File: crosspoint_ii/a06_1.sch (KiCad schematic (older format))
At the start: 38 parts, among them U6001 74HC27, U6002 74HC02, U6003 74HC27, U6004 74LVC07, U6005 74HC02, U6006 74HC04, U6007 74HC27, U6008 74HC27, U6009 74HC02, U6010 74HC04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

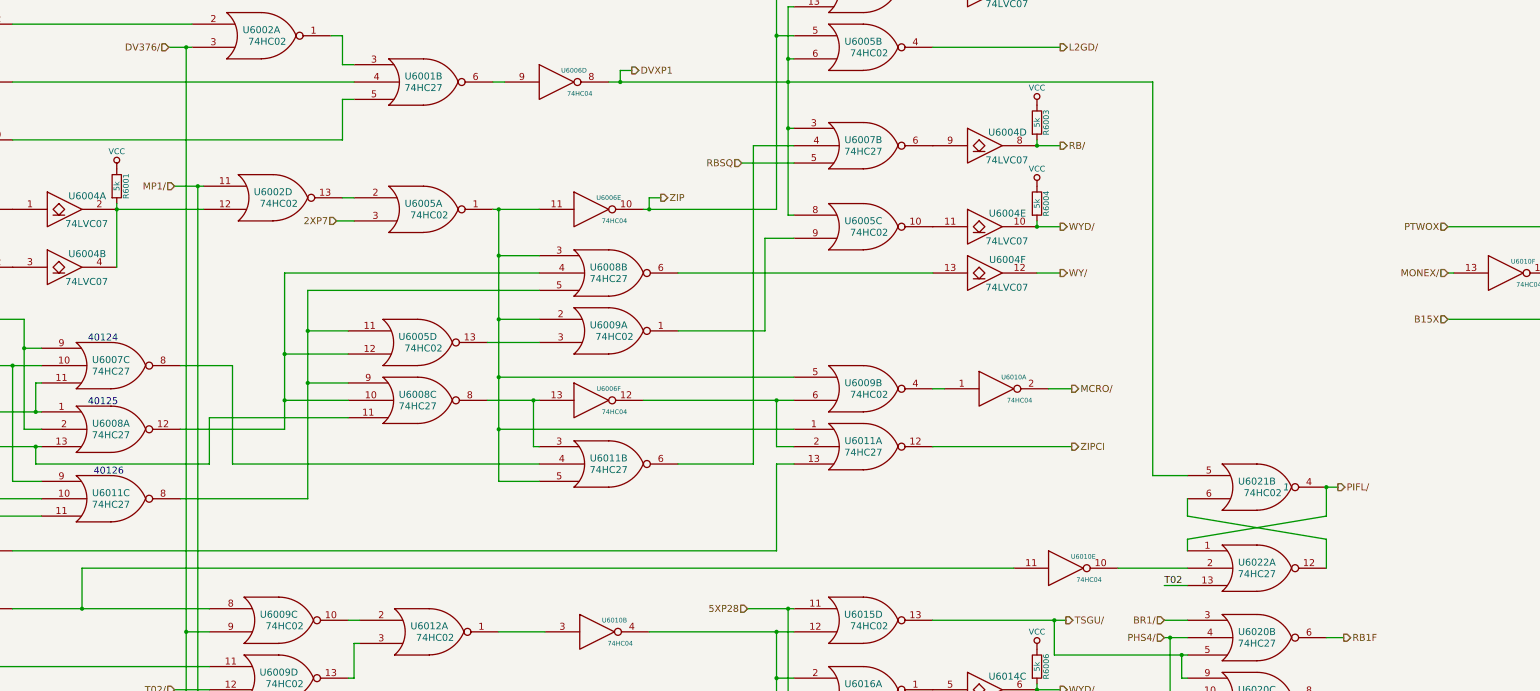
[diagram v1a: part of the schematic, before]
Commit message: Tied in module 6 and corrected a handful of naming/routing errors... most notably some missing gates from A06-1
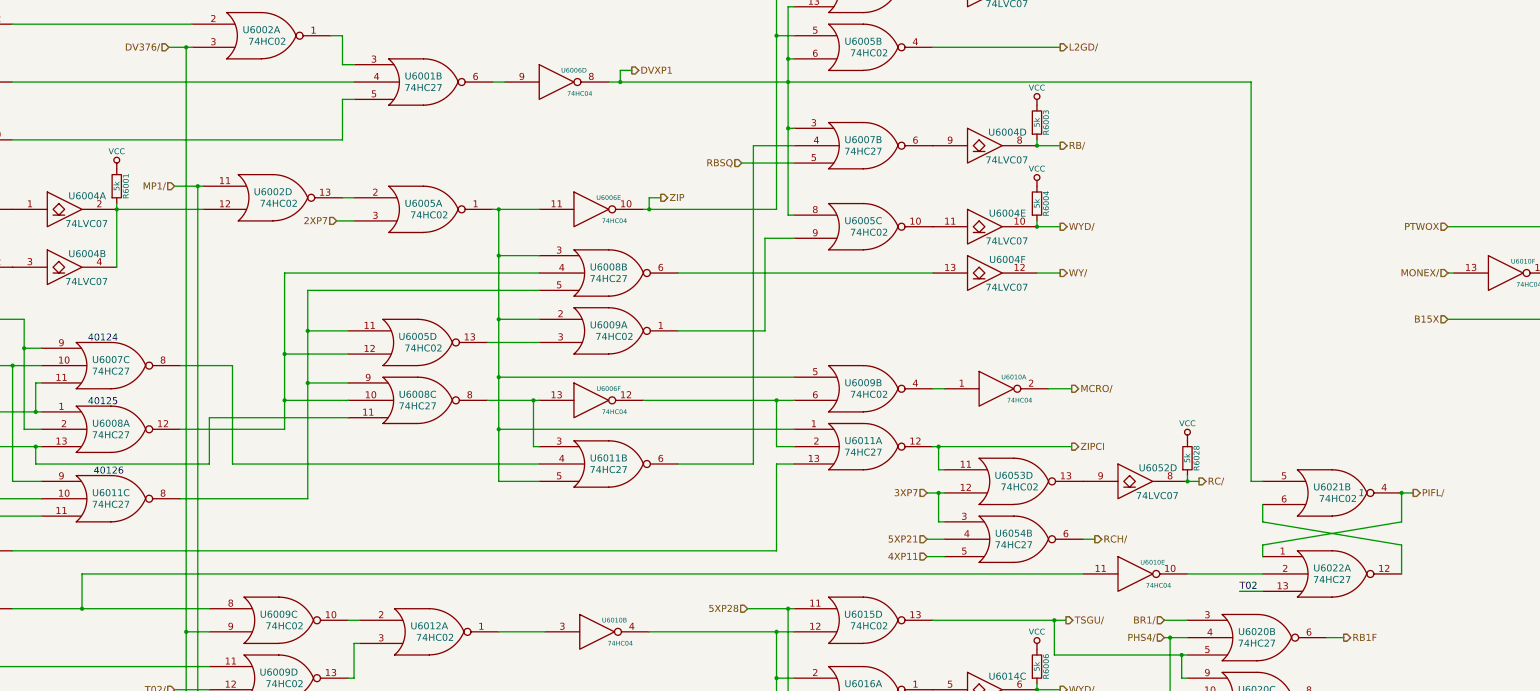
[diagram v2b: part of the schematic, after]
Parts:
- added R6028: 5k, symbol R
- added U6052: 74LVC07, symbol 74LVC07
- added U6053: 74HC02, symbol 74HC02
- added U6054: 74HC27, symbol 74HC27
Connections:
- net GND: now also U6052.7 (GND), U6053.7 (GND), U6054.7 (GND)
- net VCC: now also R6028.1, U6052.14 (VCC), U6053.14 (VCC), U6054.14 (VCC)
- net ZIPCI: now also U6053.11
- new net: U6052.9, U6053.13
- new net 3XP7: U6053.12, U6054.3
- new net 4XP11: U6054.5
- new net 5XP21: U6054.4
- new net RC/: R6028.2, U6052.8
- new net RCH/: U6054.6
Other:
- moved on the sheet: U6010E, U6021B, U6022A
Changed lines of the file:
@@
 $EndComp
 $Comp
-L VCC #PWR07
+L VCC #PWR03
 U 1 1 5687E325
 P 4400 2600
-F 0 "#PWR07" H 4400 2450 50  0001 C CNN
+F 0 "#PWR03" H 4400 2450 50  0001 C CNN
 F 1 "VCC" H 4400 2750 50  0000 C CNN
 F 2 "" H 4400 2600 60  0000 C CNN
@@
 $EndComp
 $Comp
-L VCC #PWR08
+L VCC #PWR04
 U 1 1 56881A2B
 P 12350 700
-F 0 "#PWR08" H 12350 550 50  0001 C CNN
+F 0 "#PWR04" H 12350 550 50  0001 C CNN
 F 1 "VCC" H 12350 850 50  0000 C CNN
 F 2 "" H 12350 700 60  0000 C CNN
@@
 $EndComp
 $Comp
-L VCC #PWR09
+L VCC #PWR05
 U 1 1 56883547
 P 12350 2050
-F 0 "#PWR09" H 12350 1900 50  0001 C CNN
+F 0 "#PWR05" H 12350 1900 50  0001 C CNN
 F 1 "VCC" H 12350 2200 50  0000 C CNN
 F 2 "" H 12350 2050 60  0000 C CNN
@@
 $EndComp
 $Comp
-L VCC #PWR010
+L VCC #PWR06
 U 1 1 56884333
 P 12350 2750
-F 0 "#PWR010" H 12350 2600 50  0001 C CNN
+F 0 "#PWR06" H 12350 2600 50  0001 C CNN
 F 1 "VCC" H 12350 2900 50  0000 C CNN
 F 2 "" H 12350 2750 60  0000 C CNN
@@
 $EndComp
 $Comp
-L VCC #PWR011
+L VCC #PWR07
 U 1 1 568AA059
 P 4400 7950
-F 0 "#PWR011" H 4400 7800 50  0001 C CNN
+F 0 "#PWR07" H 4400 7800 50  0001 C CNN
 F 1 "VCC" H 4400 8100 50  0000 C CNN
 F 2 "" H 4400 7950 60  0000 C CNN
@@
 $EndComp
 $Comp
-L VCC #PWR012
+L VCC #PWR08
 U 1 1 568B96C1
 P 12350 6750
-F 0 "#PWR012" H 12350 6600 50  0001 C CNN
+F 0 "#PWR08" H 12350 6600 50  0001 C CNN
 F 1 "VCC" H 12350 6900 50  0000 C CNN
 F 2 "" H 12350 6750 60  0000 C CNN
@@
 $EndComp
 $Comp
-L VCC #PWR013
+L VCC #PWR09
 U 1 1 568BD3AF
 P 12350 7500
-F 0 "#PWR013" H 12350 7350 50  0001 C CNN
+F 0 "#PWR09" H 12350 7350 50  0001 C CNN
 F 1 "VCC" H 12350 7650 50  0000 C CNN
 F 2 "" H 12350 7500 60  0000 C CNN
@@
 $EndComp
 $Comp
-L VCC #PWR014
+L VCC #PWR010
 U 1 1 568BF167
 P 12350 8200
-F 0 "#PWR014" H 12350 8050 50  0001 C CNN
+F 0 "#PWR010" H 12350 8050 50  0001 C CNN
 F 1 "VCC" H 12350 8350 50  0000 C CNN
 F 2 "" H 12350 8200 60  0000 C CNN
@@
 $EndComp
 $Comp
-L VCC #PWR015
+L VCC #PWR011
 U 1 1 568BFF2A
 P 12350 8900
-F 0 "#PWR015" H 12350 8750 50  0001 C CNN
+F 0 "#PWR011" H 12350 8750 50  0001 C CNN
 F 1 "VCC" H 12350 9050 50  0000 C CNN
 F 2 "" H 12350 8900 60  0000 C CNN
@@
 $EndComp
 $Comp
-L VCC #PWR016
+L VCC #PWR012
 U 1 1 568D20A8
 P 12350 9600
-F 0 "#PWR016" H 12350 9450 50  0001 C CNN
+F 0 "#PWR012" H 12350 9450 50  0001 C CNN
 F 1 "VCC" H 12350 9750 50  0000 C CNN
 F 2 "" H 12350 9600 60  0000 C CNN
@@
 	10200 1200 10200 3000
 Wire Wire Line
-	8650 1850 13350 1850
+	8650 1850 14200 1850
 Wire Wire Line
 	10200 1650 10250 1650
@@
 $EndComp
 $Comp
-L VCC #PWR017
+L VCC #PWR013
 U 1 1 568E688E
 P 12350 10700
-F 0 "#PWR017" H 12350 10550 50  0001 C CNN
+F 0 "#PWR013" H 12350 10550 50  0001 C CNN
 F 1 "VCC" H 12350 10850 50  0000 C CNN
 F 2 "" H 12350 10700 60  0000 C CNN
@@
 $EndComp
 $Comp
-L VCC #PWR018
+L VCC #PWR014
 U 1 1 568E71E1
 P 12350 11400
-F 0 "#PWR018" H 12350 11250 50  0001 C CNN
+F 0 "#PWR014" H 12350 11250 50  0001 C CNN
 F 1 "VCC" H 12350 11550 50  0000 C CNN
 F 2 "" H 12350 11400 60  0000 C CNN
@@
 $EndComp
 $Comp
-L VCC #PWR019
+L VCC #PWR015
 U 1 1 568E86FE
 P 12350 12100
-F 0 "#PWR019" H 12350 11950 50  0001 C CNN
+F 0 "#PWR015" H 12350 11950 50  0001 C CNN
 F 1 "VCC" H 12350 12250 50  0000 C CNN
 F 2 "" H 12350 12100 60  0000 C CNN
@@
 DVXP1
 Wire Wire Line
-	4100 6400 4100 6050
-Wire Wire Line
-	4100 6050 12150 6050
+	4100 6400 4100 6100
+Wire Wire Line
+	4100 6100 12750 6100
 Connection ~ 4100 6400
 Wire Wire Line
@@
 L 74HC04 U6010
 U 5 1 568FA6F1
-P 12600 6050
-F 0 "U6010" H 12750 6150 40  0000 C CNN
-F 1 "74HC04" H 12800 5950 40  0000 C CNN
-F 2 "" H 12600 6050 60  0000 C CNN
-F 3 "" H 12600 6050 60  0000 C CNN
-	5    12600 6050
+P 13200 6100
+F 0 "U6010" H 13350 6200 40  0000 C CNN
+F 1 "74HC04" H 13400 6000 40  0000 C CNN
+F 2 "" H 13200 6100 60  0000 C CNN
+F 3 "" H 13200 6100 60  0000 C CNN
+	5    13200 6100
 	1    0    0    -1
 $EndComp
@@
 L 74HC27 U6022
 U 1 1 568FE0E3
-P 14250 6050
-F 0 "U6022" H 14250 6100 60  0000 C CNN
-F 1 "74HC27" H 14250 6000 60  0000 C CNN
-F 2 "" H 14250 6050 60  0000 C CNN
-F 3 "" H 14250 6050 60  0000 C CNN
-	1    14250 6050
-	1    0    0    -1
-$EndComp
-Wire Wire Line
-	13050 6050 13650 6050
-Wire Wire Line
-	13650 6200 13450 6200
-Text Label 13450 6200 0    60   ~ 0
+P 14900 6100
+F 0 "U6022" H 14900 6150 60  0000 C CNN
+F 1 "74HC27" H 14900 6050 60  0000 C CNN
+F 2 "" H 14900 6100 60  0000 C CNN
+F 3 "" H 14900 6100 60  0000 C CNN
+	1    14900 6100
+	1    0    0    -1
+$EndComp
+Wire Wire Line
+	13650 6100 14300 6100
+Wire Wire Line
+	14300 6250 14100 6250
+Text Label 14100 6250 0    60   ~ 0
 T02
 $Comp
 L 74HC02 U6021
 U 2 1 569094BF
-P 14250 5350
-F 0 "U6021" H 14250 5400 60  0000 C CNN
-F 1 "74HC02" H 14300 5300 60  0000 C CNN
-F 2 "" H 14250 5350 60  0000 C CNN
-F 3 "" H 14250 5350 60  0000 C CNN
-F 4 "1" H 14500 5350 60  0000 C CIN "Initial"
-	2    14250 5350
-	1    0    0    -1
-$EndComp
-Wire Wire Line
-	14850 6050 14850 5800
-Wire Wire Line
-	14850 5800 13650 5600
-Wire Wire Line
-	13650 5600 13650 5450
-Wire Wire Line
-	14850 5350 14850 5600
-Wire Wire Line
-	14850 5600 13650 5800
-Wire Wire Line
-	13650 5800 13650 5900
+P 14900 5400
+F 0 "U6021" H 14900 5450 60  0000 C CNN
+F 1 "74HC02" H 14950 5350 60  0000 C CNN
+F 2 "" H 14900 5400 60  0000 C CNN
+F 3 "" H 14900 5400 60  0000 C CNN
+F 4 "1" H 15150 5400 60  0000 C CIN "Initial"
+	2    14900 5400
+	1    0    0    -1
+$EndComp
+Wire Wire Line
+	15500 6100 15500 5850
+Wire Wire Line
+	15500 5850 14300 5650
+Wire Wire Line
+	14300 5650 14300 5500
+Wire Wire Line
+	15500 5400 15500 5650
+Wire Wire Line
+	15500 5650 14300 5850
+Wire Wire Line
+	14300 5850 14300 5950
 Connection ~ 8750 1850
 Connection ~ 10200 1850
 Wire Wire Line
-	13350 1850 13350 5250
-Wire Wire Line
-	13350 5250 13650 5250
-Wire Wire Line
-	14850 5350 14950 5350
-Connection ~ 14850 5350
-Text HLabel 14950 5350 2    60   Output ~ 0
+	14200 1850 14200 5300
+Wire Wire Line
+	14200 5300 14300 5300
+Wire Wire Line
+	15500 5400 15600 5400
+Connection ~ 15500 5400
+Text HLabel 15600 5400 2    60   Output ~ 0
 PIFL/
 $Comp
@@
 Text HLabel 16350 7850 2    60   Output ~ 0
 CGMC
+$Comp
+L 74HC02 U6053
+U 4 1 56A22E56
+P 12150 5300
+F 0 "U6053" H 12150 5350 60  0000 C CNN
+F 1 "74HC02" H 12200 5250 60  0000 C CNN
+F 2 "" H 12150 5300 60  0000 C CNN
+F 3 "" H 12150 5300 60  0000 C CNN
+	4    12150 5300
+	1    0    0    -1
+$EndComp
+Wire Wire Line
+	11550 5200 11500 5200
+Wire Wire Line
+	11500 5200 11500 5000
+Connection ~ 11500 5000
+$Comp
+L 74LVC07 U6052
+U 4 1 56A24714
+P 13200 5300
+F 0 "U6052" H 13395 5415 60  0000 C CNN
+F 1 "74LVC07" H 13390 5175 60  0000 C CNN
+F 2 "" H 13200 5300 60  0000 C CNN
+F 3 "" H 13200 5300 60  0000 C CNN
+	4    13200 5300
+	1    0    0    -1
+$EndComp
+$Comp
+L R R6028
+U 1 1 56A249BC
+P 13650 5100
+F 0 "R6028" V 13730 5100 50  0000 C CNN
+F 1 "5k" V 13650 5100 50  0000 C CNN
+F 2 "" V 13580 5100 30  0000 C CNN
+F 3 "" H 13650 5100 30  0000 C CNN
+	1    13650 5100
+	1    0    0    -1
+$EndComp
+$Comp
+L VCC #PWR016
+U 1 1 56A249C2
+P 13650 4950
+F 0 "#PWR016" H 13650 4800 50  0001 C CNN
+F 1 "VCC" H 13650 5100 50  0000 C CNN
+F 2 "" H 13650 4950 60  0000 C CNN
+F 3 "" H 13650 4950 60  0000 C CNN
+	1    13650 4950
+	1    0    0    -1
+$EndComp
+Wire Wire Line
+	13650 5250 13650 5300
+Connection ~ 13650 5300
+Wire Wire Line
+	13650 5300 13750 5300
+Text HLabel 13750 5300 2    60   Output ~ 0
+RC/
+Wire Wire Line
+	11400 5400 11550 5400
+Text HLabel 11400 5400 0    60   Input ~ 0
+3XP7
+$Comp
+L 74HC27 U6054
+U 2 1 56A2572E
+P 12150 5800
+F 0 "U6054" H 12150 5850 60  0000 C CNN
+F 1 "74HC27" H 12150 5750 60  0000 C CNN
+F 2 "" H 12150 5800 60  0000 C CNN
+F 3 "" H 12150 5800 60  0000 C CNN
+	2    12150 5800
+	1    0    0    -1
+$EndComp
+Wire Wire Line
+	11500 5400 11500 5650
+Wire Wire Line
+	11500 5650 11550 5650
+Connection ~ 11500 5400
+Wire Wire Line
+	12750 5800 12850 5800
+Text HLabel 12850 5800 2    60   Output ~ 0
+RCH/
+Text HLabel 11400 5800 0    60   Input ~ 0
+5XP21
+Wire Wire Line
+	11400 5800 11550 5800
+Text HLabel 11400 5950 0    60   Input ~ 0
+4XP11
+Wire Wire Line
+	11400 5950 11550 5950
 $EndSCHEMATC

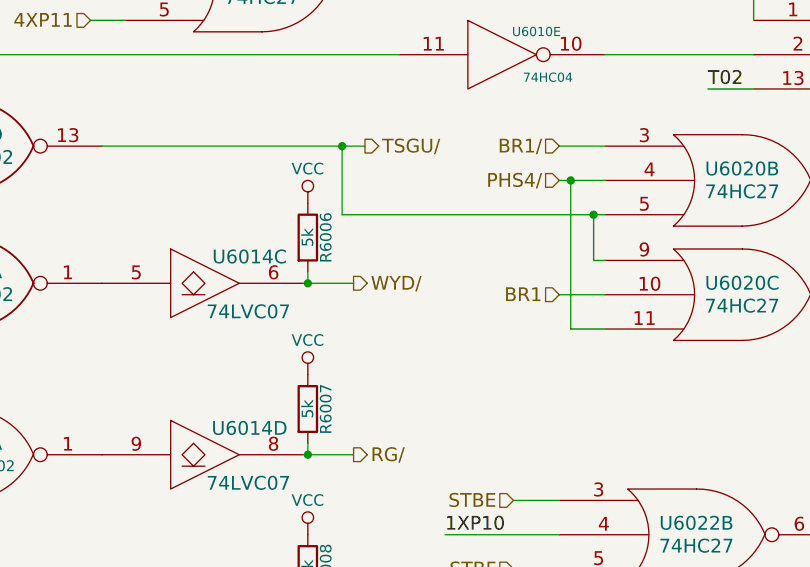
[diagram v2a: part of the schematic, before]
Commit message: Tied in module 7, and corrected lots of errors.
Off the top of my head:
* T12DC/ not actually connected to restart logic in A02-2
* IC12/ and IC13 schematic errors
* Lots of gates moved from later modules up to modules 2-7
* YT0..7 logic dropped from 7, it belongs in 14
* Lots of missing signal breakouts
* ...probably some other things, I should keep a list as I go

All control pulses associated with GOJ1 now behave correctly during
GOJ1.
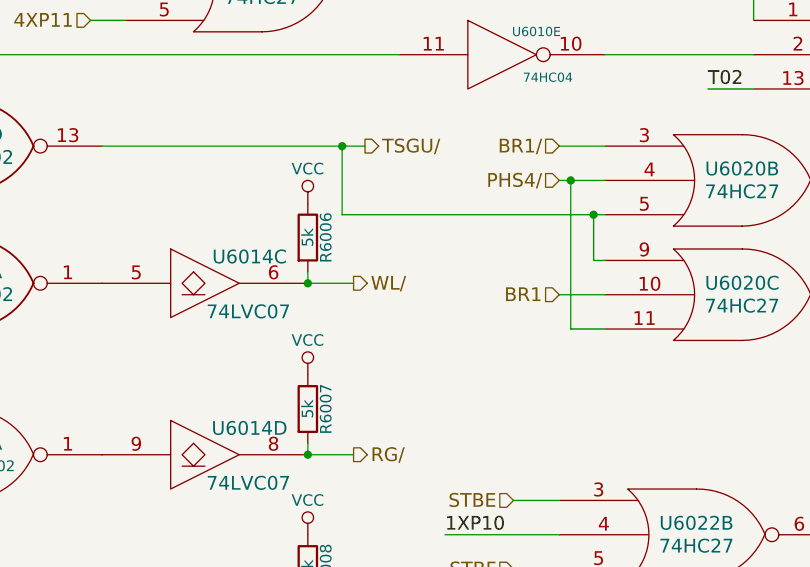
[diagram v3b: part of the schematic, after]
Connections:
- net WYD/: no longer R6006.2, U6014.6
- new net WL/: R6006.2, U6014.6
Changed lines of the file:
@@
 $EndComp
 $Comp
-L VCC #PWR03
+L VCC #PWR04
 U 1 1 5687E325
 P 4400 2600
-F 0 "#PWR03" H 4400 2450 50  0001 C CNN
+F 0 "#PWR04" H 4400 2450 50  0001 C CNN
 F 1 "VCC" H 4400 2750 50  0000 C CNN
 F 2 "" H 4400 2600 60  0000 C CNN
@@
 $EndComp
 $Comp
-L VCC #PWR04
+L VCC #PWR05
 U 1 1 56881A2B
 P 12350 700
-F 0 "#PWR04" H 12350 550 50  0001 C CNN
+F 0 "#PWR05" H 12350 550 50  0001 C CNN
 F 1 "VCC" H 12350 850 50  0000 C CNN
 F 2 "" H 12350 700 60  0000 C CNN
@@
 $EndComp
 $Comp
-L VCC #PWR05
+L VCC #PWR06
 U 1 1 56883547
 P 12350 2050
-F 0 "#PWR05" H 12350 1900 50  0001 C CNN
+F 0 "#PWR06" H 12350 1900 50  0001 C CNN
 F 1 "VCC" H 12350 2200 50  0000 C CNN
 F 2 "" H 12350 2050 60  0000 C CNN
@@
 $EndComp
 $Comp
-L VCC #PWR06
+L VCC #PWR07
 U 1 1 56884333
 P 12350 2750
-F 0 "#PWR06" H 12350 2600 50  0001 C CNN
+F 0 "#PWR07" H 12350 2600 50  0001 C CNN
 F 1 "VCC" H 12350 2900 50  0000 C CNN
 F 2 "" H 12350 2750 60  0000 C CNN
@@
 $EndComp
 $Comp
-L VCC #PWR07
+L VCC #PWR08
 U 1 1 568AA059
 P 4400 7950
-F 0 "#PWR07" H 4400 7800 50  0001 C CNN
+F 0 "#PWR08" H 4400 7800 50  0001 C CNN
 F 1 "VCC" H 4400 8100 50  0000 C CNN
 F 2 "" H 4400 7950 60  0000 C CNN
@@
 $EndComp
 $Comp
-L VCC #PWR08
+L VCC #PWR09
 U 1 1 568B96C1
 P 12350 6750
-F 0 "#PWR08" H 12350 6600 50  0001 C CNN
+F 0 "#PWR09" H 12350 6600 50  0001 C CNN
 F 1 "VCC" H 12350 6900 50  0000 C CNN
 F 2 "" H 12350 6750 60  0000 C CNN
@@
 $EndComp
 Text HLabel 12550 7100 2    60   Output ~ 0
-WYD/
+WL/
 Text HLabel 9800 7200 0    60   Input ~ 0
 5XP12
@@
 $EndComp
 $Comp
-L VCC #PWR09
+L VCC #PWR010
 U 1 1 568BD3AF
 P 12350 7500
-F 0 "#PWR09" H 12350 7350 50  0001 C CNN
+F 0 "#PWR010" H 12350 7350 50  0001 C CNN
 F 1 "VCC" H 12350 7650 50  0000 C CNN
 F 2 "" H 12350 7500 60  0000 C CNN
@@
 $EndComp
 $Comp
-L VCC #PWR010
+L VCC #PWR011
 U 1 1 568BF167
 P 12350 8200
-F 0 "#PWR010" H 12350 8050 50  0001 C CNN
+F 0 "#PWR011" H 12350 8050 50  0001 C CNN
 F 1 "VCC" H 12350 8350 50  0000 C CNN
 F 2 "" H 12350 8200 60  0000 C CNN
@@
 $EndComp
 $Comp
-L VCC #PWR011
+L VCC #PWR012
 U 1 1 568BFF2A
 P 12350 8900
-F 0 "#PWR011" H 12350 8750 50  0001 C CNN
+F 0 "#PWR012" H 12350 8750 50  0001 C CNN
 F 1 "VCC" H 12350 9050 50  0000 C CNN
 F 2 "" H 12350 8900 60  0000 C CNN
@@
 $EndComp
 $Comp
-L VCC #PWR012
+L VCC #PWR013
 U 1 1 568D20A8
 P 12350 9600
-F 0 "#PWR012" H 12350 9450 50  0001 C CNN
+F 0 "#PWR013" H 12350 9450 50  0001 C CNN
 F 1 "VCC" H 12350 9750 50  0000 C CNN
 F 2 "" H 12350 9600 60  0000 C CNN
@@
 $EndComp
 $Comp
-L VCC #PWR013
+L VCC #PWR014
 U 1 1 568E688E
 P 12350 10700
-F 0 "#PWR013" H 12350 10550 50  0001 C CNN
+F 0 "#PWR014" H 12350 10550 50  0001 C CNN
 F 1 "VCC" H 12350 10850 50  0000 C CNN
 F 2 "" H 12350 10700 60  0000 C CNN
@@
 $EndComp
 $Comp
-L VCC #PWR014
+L VCC #PWR015
 U 1 1 568E71E1
 P 12350 11400
-F 0 "#PWR014" H 12350 11250 50  0001 C CNN
+F 0 "#PWR015" H 12350 11250 50  0001 C CNN
 F 1 "VCC" H 12350 11550 50  0000 C CNN
 F 2 "" H 12350 11400 60  0000 C CNN
@@
 $EndComp
 $Comp
-L VCC #PWR015
+L VCC #PWR016
 U 1 1 568E86FE
 P 12350 12100
-F 0 "#PWR015" H 12350 11950 50  0001 C CNN
+F 0 "#PWR016" H 12350 11950 50  0001 C CNN
 F 1 "VCC" H 12350 12250 50  0000 C CNN
 F 2 "" H 12350 12100 60  0000 C CNN
@@
 $EndComp
 $Comp
-L VCC #PWR016
+L VCC #PWR017
 U 1 1 56A249C2
 P 13650 4950
-F 0 "#PWR016" H 13650 4800 50  0001 C CNN
+F 0 "#PWR017" H 13650 4800 50  0001 C CNN
 F 1 "VCC" H 13650 5100 50  0000 C CNN
 F 2 "" H 13650 4950 60  0000 C CNN

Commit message: Tied in module 8, and corrected lots of initial conditions.
The registers and ALU appear to work now, with TC0 and STD2 shuffling things around correctly, and Z counting up as instructions execute.
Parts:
- added U6055, U6056: 74HC04, symbol 74HC04
- U6003, U6005, U6007, U6012, U6013, U6015, U6016, U6017, U6021: Initial (none) -> 1
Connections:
- net GND: now also U6055.7 (GND), U6055.7 (GND), U6055.7 (GND), U6055.7 (GND), U6055.7 (GND), U6055.7 (GND), U6056.7 (GND)
- net L02A/: now also U6055.8
- net L15A/: now also U6055.12
- net VCC: now also U6055.14 (VCC), U6055.14 (VCC), U6055.14 (VCC), U6055.14 (VCC), U6055.14 (VCC), U6055.14 (VCC), U6056.14 (VCC)
- net at U6008.6: now also U6056.1; no longer U6004.13
- new net: U6004.13, U6056.2
- new net: U6055.6, U6055.9
- new net: U6055.10, U6055.13
- new net L02/: U6055.5
- new net L15/: U6055.11
- new net R1C: U6055.2
- new net R1C/: U6055.1
- new net RB1: U6055.4
- new net RB1/: U6055.3
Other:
- moved on the sheet: R6001, R6002, R6003, R6004, R6005, R6006, R6007, R6008, R6009, R6010, R6011, R6012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
